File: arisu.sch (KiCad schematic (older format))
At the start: 40 parts, among them J1 USB_B_Micro, J10 PF6, J11 PF7, J12 VCC, J13 D+, J14 D-, J15 GND, J2 MISO, J3 VCC, J4 SCK, J5 MOSI, J6 RES, J7 GND, J8 PF4, J9 PF5, U1 USBLC6-2SC6, U2 ATmega32U4-AU, Y1 Crystal_GND24

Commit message: USB-C version of the arisu
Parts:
- removed J1: USB_B_Micro, Connectors_USB:USB_Micro-B_Molex-105017-0001, symbol Connector:USB_B_Micro
- added J1: USB_C_Receptacle_USB2.0, cftkb:USB_C_GCT_USB4085, symbol Connector:USB_C_Receptacle_USB2.0
- added R5, R6: 5.1K, Resistor_SMD:R_0805_2012Metric_Pad1.15x1.40mm_HandSolder, symbol Device:R
- U1: symbol Power_Protection:USBLC6-2SC6 -> arisu-rescue:USBLC6-2SC6-Power_Protection
- U2: symbol MCU_Microchip_ATmega:ATmega32U4-AU -> arisu-rescue:ATmega32U4-AU-MCU_Microchip_ATmega
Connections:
- wire segments 131 -> 146
- no-connect marks 4 -> 5
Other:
- moved on the sheet: J12, J13, J14, J15, R1, R2

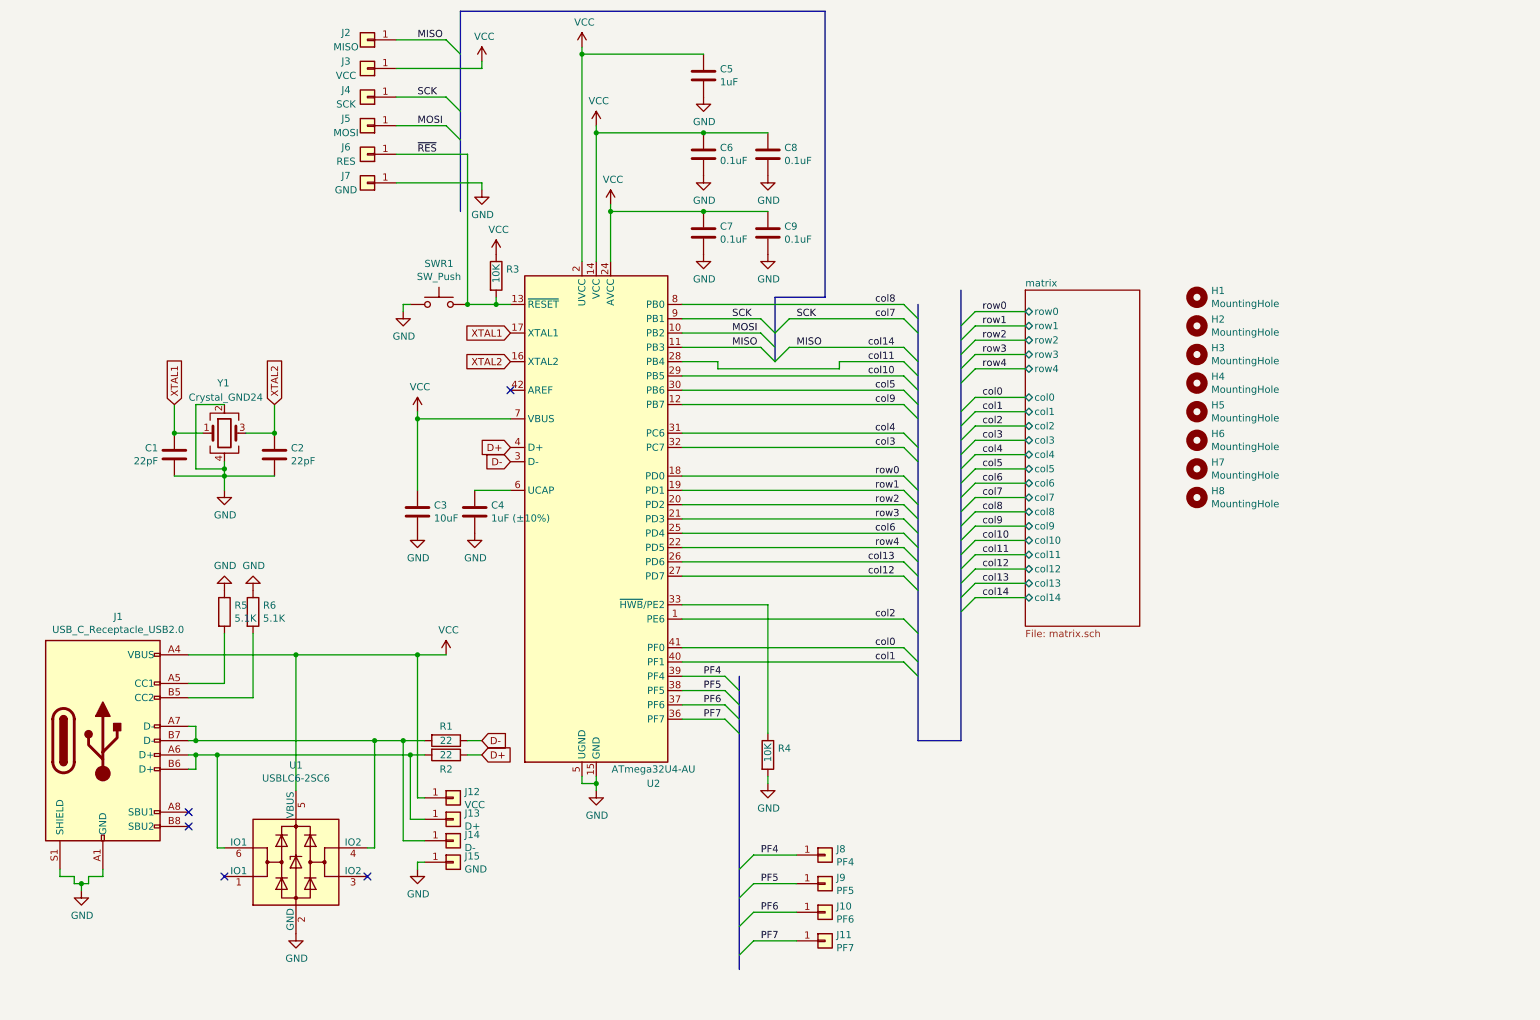
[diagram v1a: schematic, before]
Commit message: First commit with arisu using a stm32f411 and usb-c
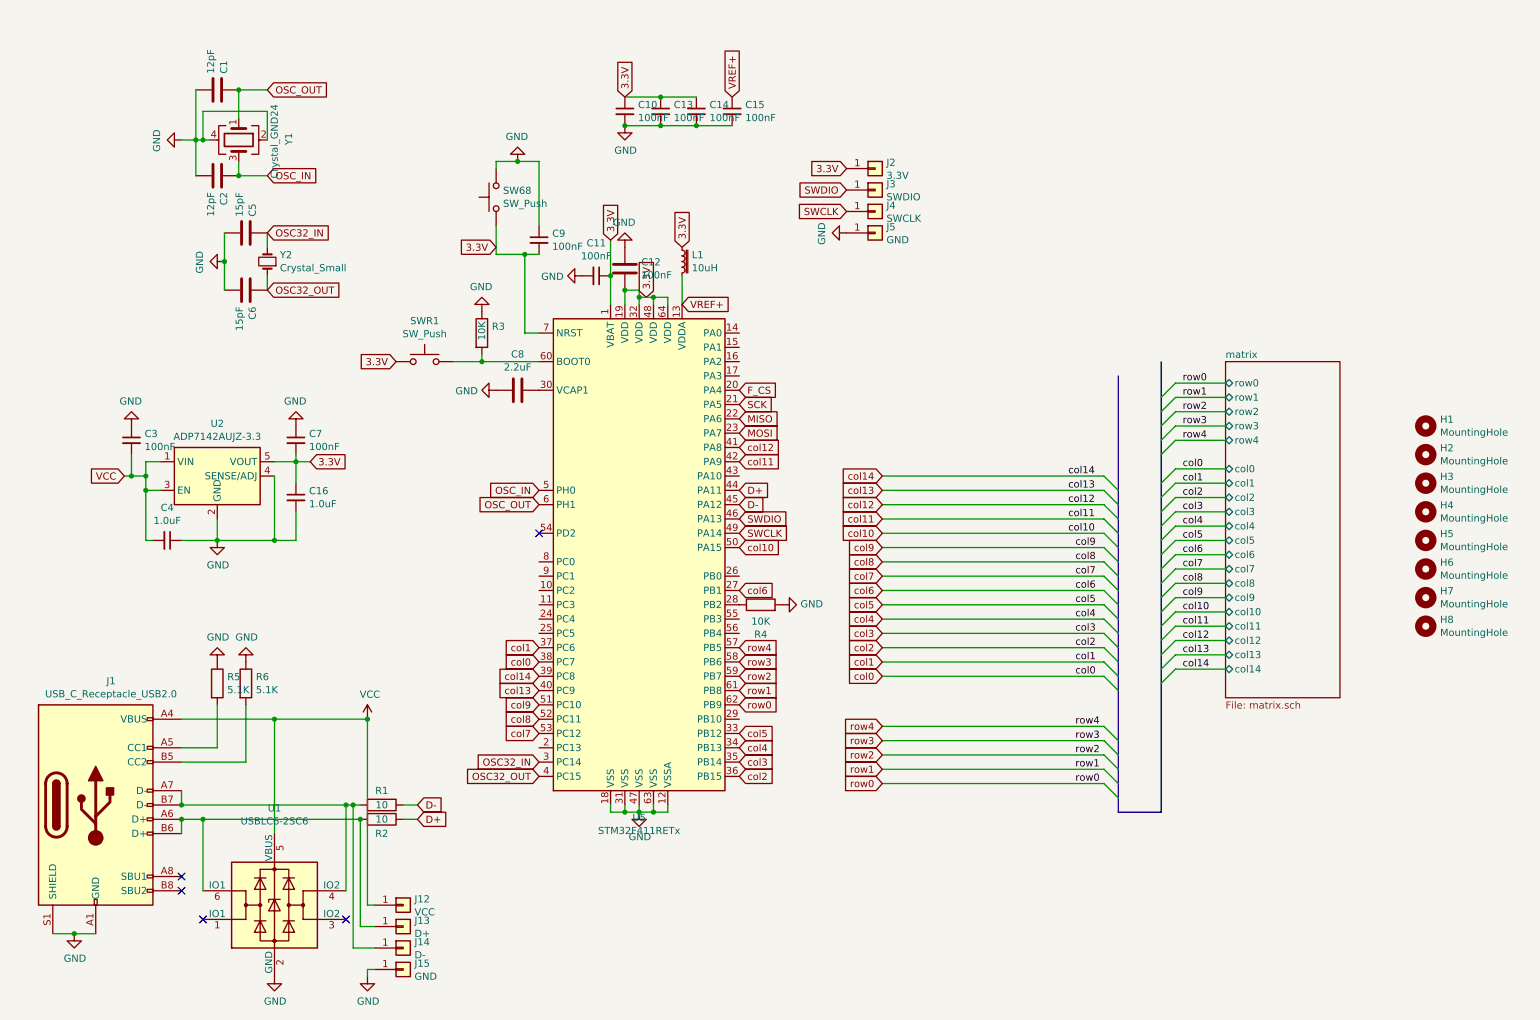
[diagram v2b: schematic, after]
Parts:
- removed C3: 10uF, Capacitors_SMD:C_0805_HandSoldering, symbol Device:C
- removed C4: 1uF (±10%), Capacitors_SMD:C_0805_HandSoldering, symbol Device:C
- removed C7, C9: 0.1uF, Capacitors_SMD:C_0805_HandSoldering, symbol Device:C
- removed J10: PF6, Pin_Headers:Pin_Header_Straight_1x01_Pitch2.54mm, symbol Connector_Generic:Conn_01x01
- removed J11: PF7, Pin_Headers:Pin_Header_Straight_1x01_Pitch2.54mm, symbol Connector_Generic:Conn_01x01
- removed J6: RES, Pin_Headers:Pin_Header_Straight_1x01_Pitch2.54mm, symbol Connector_Generic:Conn_01x01
- removed J7: GND, Pin_Headers:Pin_Header_Straight_1x01_Pitch2.54mm, symbol Connector_Generic:Conn_01x01
- removed J8: PF4, Pin_Headers:Pin_Header_Straight_1x01_Pitch2.54mm, symbol Connector_Generic:Conn_01x01
- removed J9: PF5, Pin_Headers:Pin_Header_Straight_1x01_Pitch2.54mm, symbol Connector_Generic:Conn_01x01
- removed U2: ATmega32U4-AU, Housings_QFP:TQFP-44_10x10mm_Pitch0.8mm, symbol arisu-rescue:ATmega32U4-AU-MCU_Microchip_ATmega
- added C10, C11, C13, C14, C15, C3, C7, C9: 100nF, Capacitor_SMD:C_0805_2012Metric_Pad1.15x1.40mm_HandSolder, symbol Device:C_Small
- added C12: 100nF, Capacitor_SMD:C_0805_2012Metric_Pad1.15x1.40mm_HandSolder, symbol Device:C
- added C16, C4: 1.0uF, Capacitor_SMD:C_0805_2012Metric_Pad1.15x1.40mm_HandSolder, symbol Device:C_Small
- added L1: 10uH, Inductor_SMD:L_0805_2012Metric_Pad1.15x1.40mm_HandSolder, symbol Device:L_Core_Iron_Small
- added SW68: SW_Push, Button_Switch_SMD:SW_SPST_TL3342, symbol Switch:SW_Push
- added U2: ADP7142AUJZ-3.3, Package_TO_SOT_SMD:TSOT-23-5, symbol Regulator_Linear:ADP7142AUJZ-3.3
- added U5: STM32F411RETx, Package_QFP:LQFP-64_10x10mm_P0.5mm, symbol MCU_ST_STM32F4:STM32F411RETx
- added Y2: Crystal_Small, Crystal:Crystal_SMD_MicroCrystal_CC7V-T1A-2Pin_3.2x1.5mm_HandSoldering, symbol Device:Crystal_Small
- C1, C2: value 22pF -> 12pF; footprint Capacitors_SMD:C_0805_HandSoldering -> Capacitor_SMD:C_0805_2012Metric_Pad1.15x1.40mm_HandSolder
- C5: value 1uF -> 15pF; footprint Capacitors_SMD:C_0805_HandSoldering -> Capacitor_SMD:C_0805_2012Metric_Pad1.15x1.40mm_HandSolder
- C6: value 0.1uF -> 15pF; footprint Capacitors_SMD:C_0805_HandSoldering -> Capacitor_SMD:C_0805_2012Metric_Pad1.15x1.40mm_HandSolder
- C8: value 0.1uF -> 2.2uF; footprint Capacitors_SMD:C_0805_HandSoldering -> Capacitor_SMD:C_0805_2012Metric_Pad1.15x1.40mm_HandSolder
- J12, J13, J14, J15: footprint Pin_Headers:Pin_Header_Straight_1x01_Pitch2.54mm -> Connector_PinHeader_2.54mm:PinHeader_1x01_P2.54mm_Vertical
- J2: value MISO -> 3.3V; footprint Pin_Headers:Pin_Header_Straight_1x01_Pitch2.54mm -> Connector_PinHeader_2.54mm:PinHeader_1x01_P2.54mm_Vertical
- J3: value VCC -> SWDIO; footprint Pin_Headers:Pin_Header_Straight_1x01_Pitch2.54mm -> Connector_PinHeader_2.54mm:PinHeader_1x01_P2.54mm_Vertical
- J4: value SCK -> SWCLK; footprint Pin_Headers:Pin_Header_Straight_1x01_Pitch2.54mm -> Connector_PinHeader_2.54mm:PinHeader_1x01_P2.54mm_Vertical
- J5: value MOSI -> GND; footprint Pin_Headers:Pin_Header_Straight_1x01_Pitch2.54mm -> Connector_PinHeader_2.54mm:PinHeader_1x01_P2.54mm_Vertical
- R1, R2: value 22 -> 10; footprint Resistors_SMD:R_0805_HandSoldering -> Resistor_SMD:R_0805_2012Metric_Pad1.15x1.40mm_HandSolder
- R3, R4: footprint Resistors_SMD:R_0805_HandSoldering -> Resistor_SMD:R_0805_2012Metric_Pad1.15x1.40mm_HandSolder
- SWR1: footprint Buttons_Switches_SMD:SW_SPST_TL3342 -> Button_Switch_SMD:SW_SPST_TL3342; LCSC Part (none) -> C318889
- U1: LCSC Part (none) -> C7519
- Y1: footprint Crystals:Crystal_SMD_SeikoEpson_FA238-4pin_3.2x2.5mm_HandSoldering -> Crystal:Crystal_SMD_SeikoEpson_TSX3225-4Pin_3.2x2.5mm_HandSoldering; LCSC Part (none) -> C91738
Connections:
- net D+: now also U5.44 (PA11)
- net D-: now also U5.45 (PA12)
- net GND: now also C5.1, J5.1 (Pin_1), R3.1, C10.2, C11.2, C12.1, C13.2, C14.2, C15.2, C16.2, C3.1, C4.1, C7.1, C9.1, SW68.2, U2.2 (GND), U2.4 (SENSE/ADJ), U5.12 (VSSA), U5.18 (VSS), U5.31 (VSS), U5.47 (VSS), U5.63 (VSS); no longer C5.2, SWR1.1
- net MISO: now also U5.22 (PA6); no longer J2.1 (Pin_1)
- net MOSI: now also U5.23 (PA7); no longer J5.1 (Pin_1)
- net SCK: now also U5.21 (PA5); no longer J4.1 (Pin_1)
- net VCC: now also C3.2, C4.2, U2.1 (VIN), U2.3 (EN); no longer C5.1, C6.1, C8.1, J3.1 (Pin_1), R3.1
- net col0: now also U5.38 (PC7)
- net col1: now also U5.37 (PC6)
- net col10: now also U5.50 (PA15)
- net col11: now also U5.42 (PA9)
- net col12: now also U5.41 (PA8)
- net col13: now also U5.40 (PC9)
- net col2: now also U5.36 (PB15)
- net col3: now also U5.35 (PB14)
- net col4: now also U5.34 (PB13)
- net col5: now also U5.33 (PB12)
- net col6: now also U5.27 (PB1)
- net col8: now also U5.52 (PC11)
- net col9: now also U5.51 (PC10)
- net row0: now also U5.62 (PB9)
- net row1: now also U5.61 (PB8)
- net row2: now also U5.59 (PB7)
- net row3: now also U5.58 (PB6)
- net row4: now also U5.57 (PB5)
- net at R4.1: now also U5.28 (PB2)
- net XTAL1 renamed OSC_OUT
- net OSC_OUT: now also U5.6 (PH1)
- net XTAL2 renamed OSC_IN
- net OSC_IN: now also U5.5 (PH0)
- net ~RES~: no longer names the net of R3.2, SWR1.2
- net ~RES~: now also U5.60 (BOOT0)
- new net: C8.1, U5.30 (VCAP1)
- new net 3.3V: C10.1, C11.1, C12.2, C13.1, C14.1, C16.1, C7.2, C9.2, J2.1 (Pin_1), L1.1, SW68.1, SWR1.1, U2.5 (VOUT), U5.1 (VBAT), U5.19 (VDD), U5.32 (VDD), U5.48 (VDD), U5.64 (VDD), U5.7 (NRST)
- new net F_CS: U5.20 (PA4)
- new net OSC32_IN: C5.2, U5.3 (PC14), Y2.2
- new net OSC32_OUT: C6.1, U5.4 (PC15), Y2.1
- new net SWCLK: J4.1 (Pin_1), U5.49 (PA14)
- new net SWDIO: J3.1 (Pin_1), U5.46 (PA13)
- new net VREF+: C15.1, L1.2, U5.13 (VDDA)
- new net col14: U5.39 (PC8)
- new net col7: U5.53 (PC12)
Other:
- moved on the sheet: C1, C2, H1, H2, H3, H4, H5, H6, H7, H8, J1, J12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
